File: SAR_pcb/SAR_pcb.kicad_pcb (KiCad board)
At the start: 4 copper layers, 99.1 x 71.1 mm, 32 parts, among them J1 Conn_Coaxial_Power, J10 Conn_Coaxial, J11 Conn_Coaxial, J13 Conn_01x10_Male, J2 Conn_Coaxial_Power, J3 Conn_Coaxial_Power, J4 Conn_Coaxial_Power, J5 Conn_Coaxial_Power, J6 Conn_01x02_Male, J7 Conn_01x02_Male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

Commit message: Added stackup PDF, corrected Board Setup in pcbnew
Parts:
- added J12: Conn_01x02, Connector_PinHeader_2.54mm:PinHeader_1x02_P2.54mm_Vertical, F.Cu at (151.9, 78.1)
- added J14: Conn_01x02, Connector_PinHeader_2.54mm:PinHeader_1x02_P2.54mm_Vertical, F.Cu at (156.5, 78.1)
- added J15: Conn_01x02, Connector_PinHeader_2.54mm:PinHeader_1x02_P2.54mm_Vertical, F.Cu at (161.2, 78.1)
- added J16: Conn_01x02, Connector_PinHeader_2.54mm:PinHeader_1x02_P2.54mm_Vertical, F.Cu at (165.8, 78.1)
- added J17: Conn_01x02, Connector_PinHeader_2.54mm:PinHeader_1x02_P2.54mm_Vertical, F.Cu at (156.5, 85.3)
- added J18: Conn_01x02, Connector_PinHeader_2.54mm:PinHeader_1x02_P2.54mm_Vertical, F.Cu at (161.2, 85.3)
- added J19: Conn_01x02, Connector_PinHeader_2.54mm:PinHeader_1x02_P2.54mm_Vertical, F.Cu at (165.8, 85.3)
- added J20: Conn_01x02, Connector_PinHeader_2.54mm:PinHeader_1x02_P2.54mm_Vertical, F.Cu at (170.5, 78.1)
- added J21: Conn_01x02, Connector_PinHeader_2.54mm:PinHeader_1x02_P2.54mm_Vertical, F.Cu at (170.5, 85.3)
- J10, J11, J9: footprint Connector_Coaxial:SMA_Amphenol_132291_Vertical -> Connector_Coaxial:SMA_Amphenol_132289_EdgeMount
- J13: value Conn_01x10_Male -> Conn_01x02; footprint Connector_Molex:Molex_KK-254_AE-6410-10A_1x10_P2.54mm_Vertical -> Connector_PinHeader_2.54mm:PinHeader_1x02_P2.54mm_Vertical
- moved J13 13.7 mm to (151.9, 85.3), turned to 0 degrees
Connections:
- J1 pad 1: VINP -> VIN-
- J13 pad 1: D9 -> GND
- J13 pad 2: D8 -> D1
- J2 pad 1: VINM -> VIN+
- U2 pad 3: VINM -> VIN-
- U2 pad 33: (no net) -> GND
- U2 pad 4: VINP -> VIN+
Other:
- net class Default: clearance 0.2 -> 0.1016; trace_width 0.25 -> 0.1016; via_dia 0.8 -> 0.3302; via_drill 0.4 -> 0.2032
- rule trace_clearance: 0.2 -> 0.1016
- rule trace_min: 0.2 -> 0.1016
- rule via_min_drill: 0.3 -> 0.2032
- rule via_min_size: 0.4 -> 0.3302

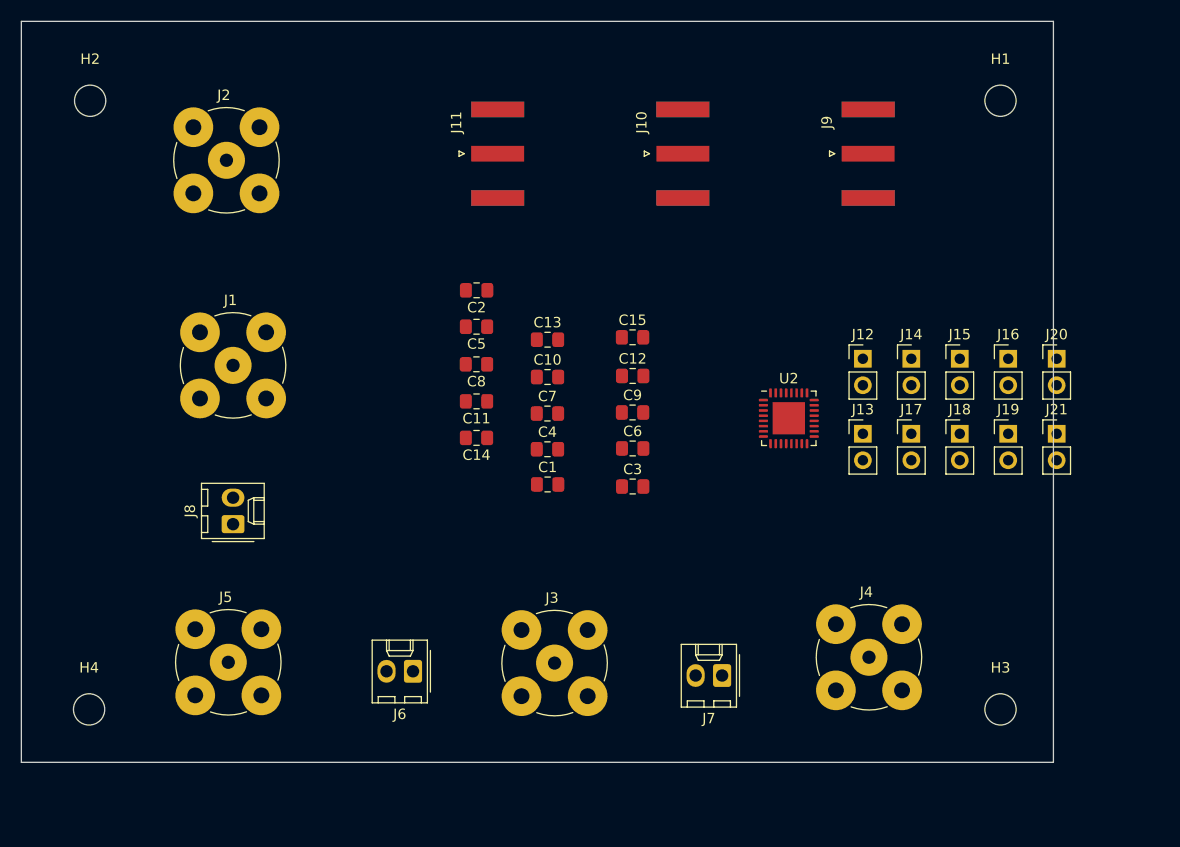
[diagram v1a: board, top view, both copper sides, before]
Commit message: added reset switch
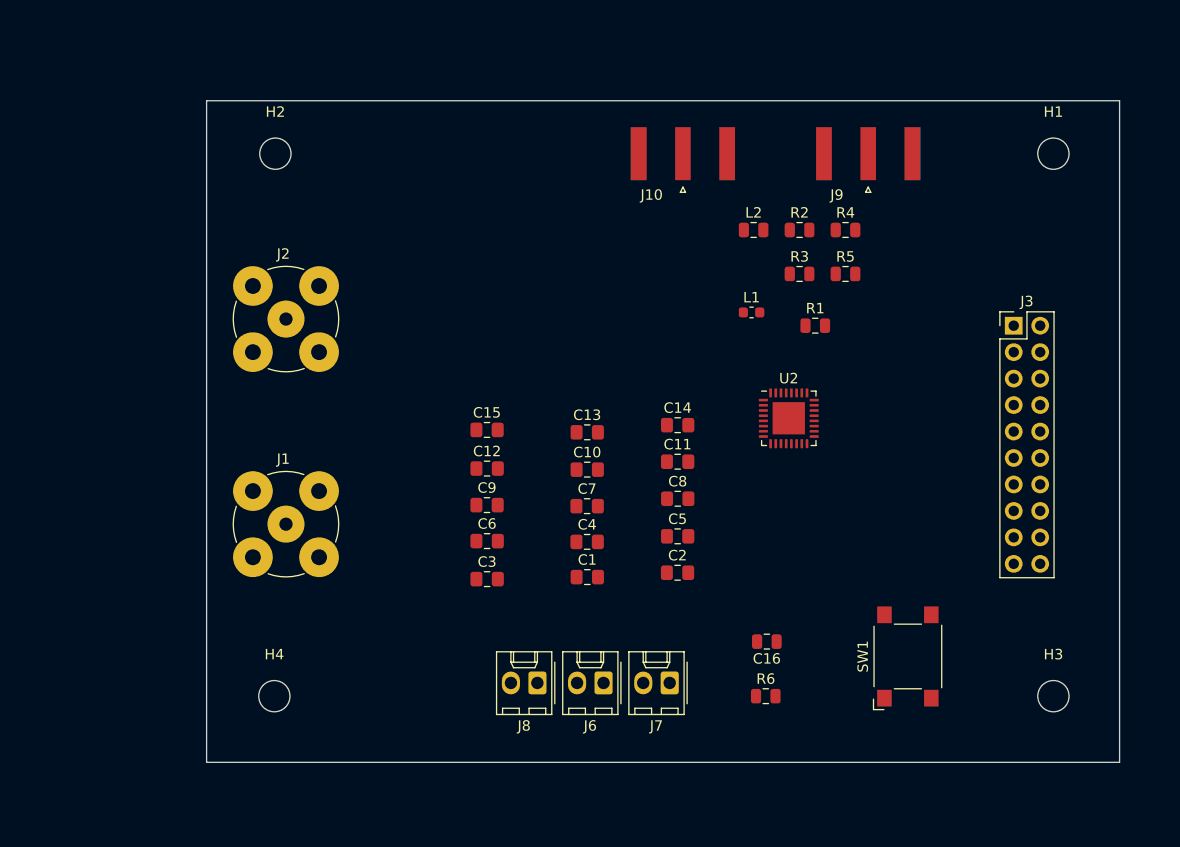
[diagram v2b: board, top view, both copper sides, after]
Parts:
- removed J11: Conn_Coaxial, Connector_Coaxial:SMA_Amphenol_132289_EdgeMount
- removed J12, J13, J14, J15, J16, J17, J18, J19, J20, J21: Conn_01x02, Connector_PinHeader_2.54mm:PinHeader_1x02_P2.54mm_Vertical
- removed J4, J5: Conn_Coaxial_Power, Connector_Coaxial:BNC_TEConnectivity_1478204_Vertical
- added C16: 1u, Capacitor_SMD:C_0805_2012Metric, F.Cu at (142.7, 105.3)
- added L1: 1 nH, Inductor_SMD:L_0603_1608Metric, F.Cu at (141.2, 73.7)
- added L2: 2.2 nH, Inductor_SMD:L_0805_2012Metric, F.Cu at (141.4, 65.7)
- added R1: 0,<20 mOhm, Resistor_SMD:R_0805_2012Metric, F.Cu at (147.3, 74.9)
- added R2: 50, Resistor_SMD:R_0805_2012Metric, F.Cu at (145.8, 65.7)
- added R3: 26.1, Resistor_SMD:R_0805_2012Metric, F.Cu at (145.8, 70.0)
- added R4: 50, Resistor_SMD:R_0805_2012Metric, F.Cu at (150.2, 65.7)
- added R5: 10, Resistor_SMD:R_0805_2012Metric, F.Cu at (150.2, 70.0)
- added R6: 1k, Resistor_SMD:R_0805_2012Metric, F.Cu at (142.6, 110.5)
- added SW1: SW_Push, Button_Switch_SMD:SW_SPST_Omron_B3FS-100xP, F.Cu at (156.2, 106.7)
- J3: value Conn_Coaxial_Power -> Conn_02x10_Top_Bottom; footprint Connector_Coaxial:BNC_TEConnectivity_1478204_Vertical -> Connector_PinHeader_2.54mm:PinHeader_2x10_P2.54mm_Vertical
- moved J3 54.7 mm to (166.4, 74.9)
- moved C2 33.3 mm to (134.1, 98.6), turned to 0 degrees
- moved J8 32.9 mm to (120.7, 109.2), turned to 180 degrees
- moved C5 27.9 mm to (134.1, 95.1), turned to 0 degrees
- moved C8 23.2 mm to (134.1, 91.5), turned to 0 degrees
- moved C11 20.2 mm to (134.1, 88.0), turned to 0 degrees
- moved C14 19.3 mm to (134.1, 84.5), turned to 0 degrees
- moved H2 18.5 mm to (95.5, 58.4)
- moved J6 18.3 mm to (127.0, 109.2)
- moved H4 17.8 mm to (95.4, 110.5)
- moved C12 16.6 mm to (115.8, 88.6)
- moved C6 16.6 mm to (115.8, 95.6)
- moved C15 16.6 mm to (115.8, 84.9)
- moved C9 16.6 mm to (115.8, 92.2)
- moved C3 16.6 mm to (115.8, 99.3)
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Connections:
- J3 pad 1: VDD -> D0
- U2 pad 27: CLK_C -> Net-(R1-Pad2)
- U2 pad 28: CLK_S -> CLK_S_FILT
- U2 pad 29: CLK -> CLK_FILT
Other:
- board size 99.1 x 71.1 mm -> 87.6 x 63.5 mm

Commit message: first draft of layout
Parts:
- U2: footprint Package_DFN_QFN:QFN-32-1EP_5x5mm_P0.5mm_EP3.1x3.1mm -> Package_DFN_QFN:QFN-32-1EP_5x5mm_P0.5mm_EP3.1x3.1mm_ThermalVias
- moved J1 22.1 mm to (95.9, 71.9)
- moved J2 14.4 mm to (95.9, 88.6)
- moved R2 12.0 mm to (133.8, 65.9)
- moved R3 12.0 mm to (133.9, 71.0), turned to 180 degrees
- moved L1 6.02 mm to (139.3, 67.9)
- moved R1 4.99 mm to (152.3, 74.3)
- moved L2 4.80 mm to (145.7, 67.9), turned to 180 degrees
- moved J3 3.50 mm to (168.8, 72.4)
- moved R4 2.07 mm to (152.3, 66.1), turned to 180 degrees
- moved R5 2.07 mm to (152.3, 70.3)
- moved J10 1.27 mm to (134.6, 57.1)
- moved J9 1.27 mm to (152.4, 57.1)
- moved C16 0.18 mm to (142.5, 105.3)
- moved U2 0.13 mm to (144.9, 83.8)
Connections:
- C16 pad 1: Net-(C16-Pad1) -> RST
- R6 pad 2: Net-(C16-Pad1) -> RST
- SW1 pad 1: Net-(C16-Pad1) -> RST
- SW1 pad 2: Net-(C16-Pad1) -> RST
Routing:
- net GND: track 0.00 -> 159.3 mm, vias 0 -> 22
- net VIN-: track 0.00 -> 51.1 mm
- net VIN+: track 0.00 -> 51.1 mm
- net RST: track 0.00 -> 47.1 mm
- net VDDPST: track 0.00 -> 39.4 mm, vias 0 -> 1
- net VDD: track 0.00 -> 37.7 mm, vias 0 -> 8
- net D9: track 0.00 -> 28.9 mm
- net D0: track 0.00 -> 28.4 mm
- net D1: track 0.00 -> 27.0 mm
- net D8: track 0.00 -> 26.8 mm
- net D2: track 0.00 -> 25.2 mm
- net D7: track 0.00 -> 24.2 mm
- net D3: track 0.00 -> 23.4 mm
- net D6: track 0.00 -> 22.6 mm
- net D4: track 0.00 -> 22.2 mm
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- added copper zone on GND, net GND
- added copper zone on VDD, net VDD
- added copper zone on F.Cu, net VDDPST
- added copper zone on B.Cu, net VREF

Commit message: Draft 2 of Layout
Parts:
- removed C10, C11, C12: 0.01, Capacitor_SMD:C_0805_2012Metric_Pad1.15x1.40mm_HandSolder
- removed C4, C5, C6: 1u, Capacitor_SMD:C_0805_2012Metric_Pad1.15x1.40mm_HandSolder
- removed C7, C8, C9: 0.1u, Capacitor_SMD:C_0805_2012Metric_Pad1.15x1.40mm_HandSolder
- removed J6, J7, J8: Conn_01x02_Male, Connector_Molex:Molex_KK-254_AE-6410-02A_1x02_P2.54mm_Vertical
- added C17: 0.01u, Capacitor_SMD:C_0805_2012Metric, F.Cu at (155.3, 92.7)
- added C18: 0.01u, Capacitor_SMD:C_0805_2012Metric, F.Cu at (145.7, 98.4)
- added C19: 0.01u, Capacitor_SMD:C_0805_2012Metric, F.Cu at (148.6, 98.5)
- added C20: 0.01u, Capacitor_SMD:C_0805_2012Metric, F.Cu at (154.3, 96.5)
- added C21: 0.01u, Capacitor_SMD:C_0805_2012Metric, F.Cu at (150.6, 98.7)
- added J4: Conn_01x06, Connector_PinSocket_2.54mm:PinSocket_1x06_P2.54mm_Vertical, F.Cu at (155.2, 115.6)
- C1, C2, C3: footprint Capacitor_SMD:C_0805_2012Metric_Pad1.15x1.40mm_HandSolder -> Capacitor_SMD:C_0805_2012Metric
- C13, C14, C15: value 0.001u -> 0.01u; footprint Capacitor_SMD:C_0805_2012Metric_Pad1.15x1.40mm_HandSolder -> Capacitor_SMD:C_0805_2012Metric
- J10, J9: footprint Connector_Coaxial:SMA_Amphenol_132289_EdgeMount -> SAR_pcb:CustomSMA
- SW1: footprint Button_Switch_SMD:SW_SPST_Omron_B3FS-100xP -> Button_Switch_THT:SW_DIP_SPSTx02_Slide_9.78x7.26mm_W7.62mm_P2.54mm
- moved H4 80.8 mm to (175.8, 118.4)
- moved H2 63.8 mm to (117.3, 118.4)
- moved H1 58.2 mm to (117.3, 82.8)
- moved J1 41.8 mm to (130.8, 94.8)
- moved J2 40.5 mm to (130.8, 109.2)
- moved C1 36.1 mm to (155.2, 119.5), turned to 270 degrees
- moved C3 35.5 mm to (145.0, 119.5), turned to 270 degrees
- moved J10 31.7 mm to (154.7, 81.7), turned to 0 degrees
- moved C15 30.7 mm to (144.1, 96.9), turned to 225 degrees
- moved R2 29.6 mm to (154.1, 87.4), turned to 315 degrees
- moved H3 28.2 mm to (175.8, 82.8)
- moved J9 26.6 mm to (142.2, 81.7), turned to 0 degrees
- moved C2 26.3 mm to (150.1, 119.5), turned to 270 degrees
- moved L1 26.0 mm to (157.3, 86.7), turned to 45 degrees
- moved R4 24.7 mm to (143.2, 89.1), turned to 225 degrees
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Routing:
- net GND: track 159.3 -> 0.16 mm, vias 22 -> 72
- net RST: track 47.1 -> 17.9 mm
- net VDDPST: track 39.4 -> 15.7 mm, vias 1 -> 6
- net VIN-: track 51.1 -> 30.3 mm
- net VIN+: track 51.1 -> 30.3 mm
- net VDD: track 37.7 -> 21.0 mm
- net CLK_S_FILT: track 19.4 -> 4.19 mm
- net VREF: track 21.9 -> 7.48 mm, vias 3 -> 2
- net CLK_FILT: track 17.0 -> 4.28 mm, vias 2 -> 0
- net Net-(R1-Pad2): track 12.8 -> 2.07 mm
- net D9: track 28.9 -> 19.2 mm
- net D8: track 26.8 -> 18.1 mm
- net D7: track 24.2 -> 15.6 mm
- net D6: track 22.6 -> 14.0 mm
- net D5: track 21.8 -> 13.5 mm
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- added copper zone on F.Cu, net GND
- added copper zone on F.Cu, net RST
- added copper zone on VDD, net VDDPST
- added copper zone on VDD, net VREF
- removed copper zone on F.Cu, net VDDPST
- removed copper zone on B.Cu, net VREF
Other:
- board size 87.6 x 63.5 mm -> 67.6 x 44.7 mm
- net class Default: via_dia 0.3302 -> 0.4572
- rule via_min_size: 0.3302 -> 0.4572

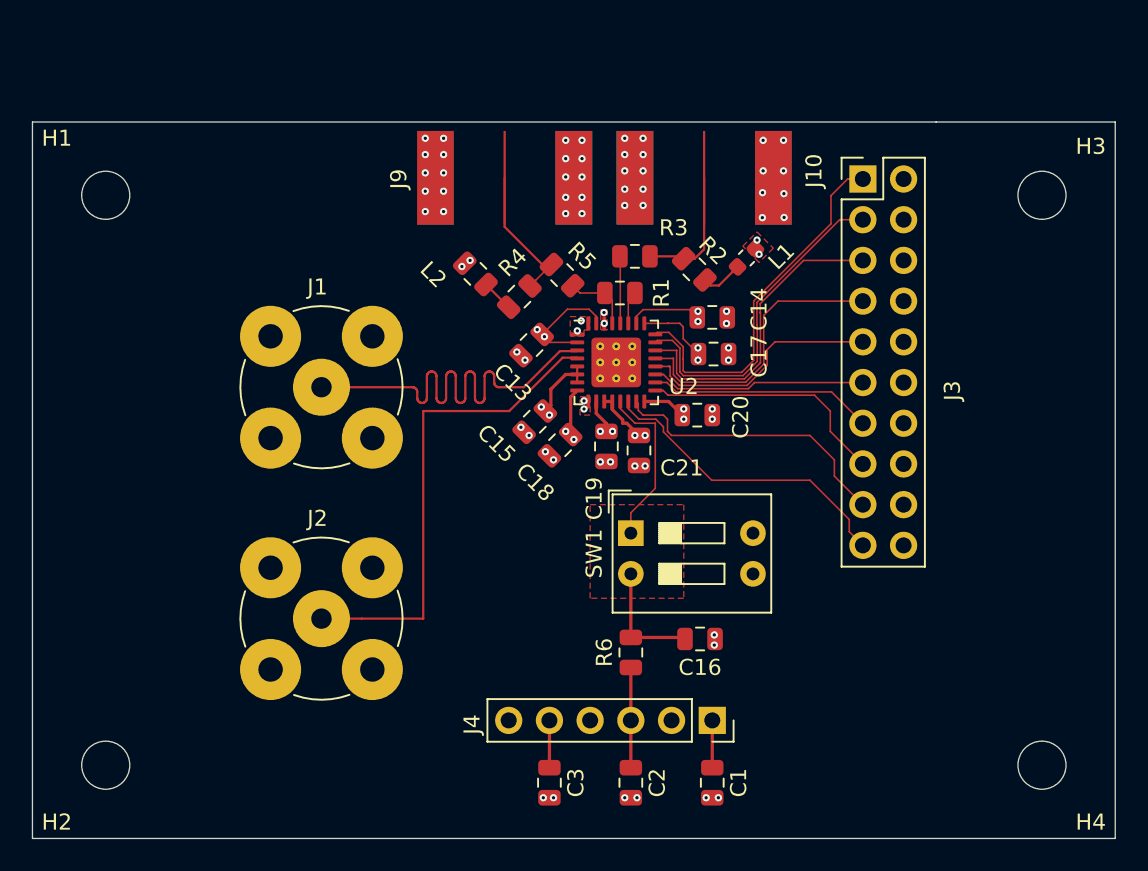
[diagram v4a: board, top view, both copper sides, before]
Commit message: Updated PCB to conform to Vanessa's recommendations
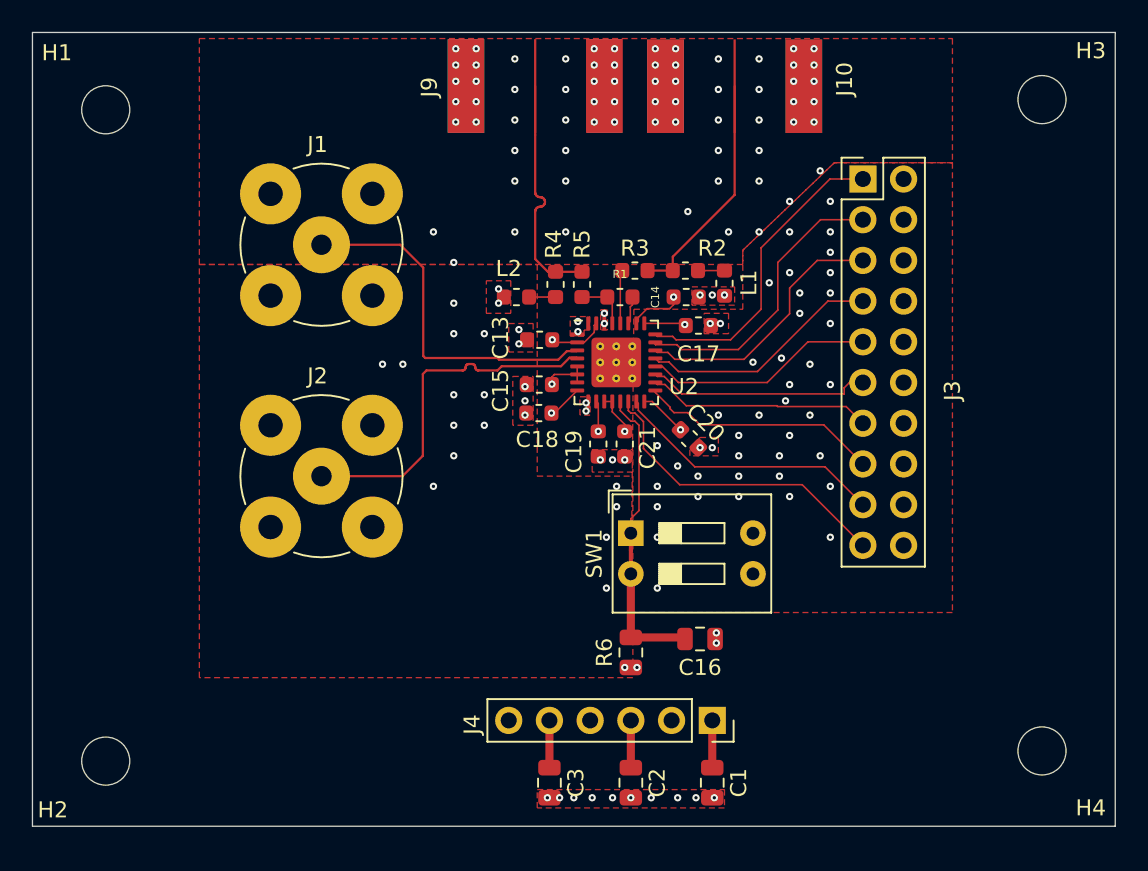
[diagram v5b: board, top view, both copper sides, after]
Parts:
- C13, C14, C15, C17, C18, C19, C20, C21: footprint Capacitor_SMD:C_0805_2012Metric -> Capacitor_SMD:C_0603_1608Metric
- L2: footprint Inductor_SMD:L_0805_2012Metric -> Inductor_SMD:L_0603_1608Metric
- R1: value 0,<20 mOhm -> 0,<0.3 mOhm; footprint Resistor_SMD:R_0805_2012Metric -> Resistor_SMD:R_0603_1608Metric
- R2, R4: value 50 -> 49.9; footprint Resistor_SMD:R_0805_2012Metric -> Resistor_SMD:R_0603_1608Metric
- R3, R5: footprint Resistor_SMD:R_0805_2012Metric -> Resistor_SMD:R_0603_1608Metric
- moved J1 8.89 mm to (130.8, 85.9)
- moved J2 8.89 mm to (130.8, 100.3)
- moved J9 6.04 mm to (144.1, 76.0)
- moved J10 6.02 mm to (156.6, 76.0)
- moved H3 5.97 mm to (175.8, 76.8)
- moved H1 5.33 mm to (117.3, 77.5)
- moved L2 2.94 mm to (143.0, 89.2), turned to 180 degrees
- moved C18 2.40 mm to (144.4, 96.4), turned to 180 degrees
- moved R4 2.38 mm to (145.4, 88.4), turned to 270 degrees
- moved C15 2.33 mm to (144.4, 94.6), turned to 180 degrees
- moved L1 2.09 mm to (156.0, 88.3), turned to 270 degrees
- moved C14 2.06 mm to (153.6, 89.2)
- moved C17 2.01 mm to (154.3, 90.9)
- moved C20 1.55 mm to (153.8, 98.0), turned to 315 degrees
- moved R5 1.37 mm to (147.1, 88.4), turned to 90 degrees
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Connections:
- net CLK renamed CLK+
- net CLK_S renamed CLK-
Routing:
- net VIN-: track 30.3 -> 22.4 mm
- net VIN+: track 30.3 -> 22.5 mm
- net VDD: track 21.0 -> 14.0 mm, vias 8 -> 4
- net CLK-: track 8.15 -> 14.7 mm
- net CLK+: track 8.85 -> 14.8 mm
- net VDDPST: track 15.7 -> 11.3 mm, vias 6 -> 5
- net D0: track 23.1 -> 19.5 mm
- net D2: track 19.8 -> 16.7 mm
- net D3: track 18.0 -> 15.1 mm
- net D1: track 21.0 -> 18.3 mm
- net VREF: track 7.48 -> 6.07 mm, vias 2 -> 1
- net RST: track 17.9 -> 19.0 mm
- net D4: track 15.5 -> 14.4 mm
- net D8: track 18.1 -> 17.1 mm
- net Net-(L1-Pad1): track 2.66 -> 1.65 mm
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- added copper zone on F.Cu, net (none)
- removed copper zone on F.Cu, net RST
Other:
- board size 67.6 x 44.7 mm -> 67.6 x 49.5 mm
